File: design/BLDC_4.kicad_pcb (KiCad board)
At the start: 4 copper layers, 55 x 77 mm, 159 parts, among them J1 Conn_01x03, J2 Conn_01x02, J3 Conn_02x06_Odd_Even, J4 Conn_01x01_Pin, J5 Conn_01x01_Pin, J6 Conn_02x06_Odd_Even, K1 SERVO, P101 CANBUS, P2 SWD, P3 PWR_COMM, Q1 IRFS7530, Q2 IRFS7530, Q3 IRFS7530, Q4 IRFS7530, Q5 IRFS7530, Q6 IRFS7530, U1 STM32F40X_LQFP64, U2 TC2117, U3 DRV8302, U4 INA826AIDR, U401 SN65HVD232, U5 AM26LV32xD, U6 OPA333AIDBVR, U7 INA826AIDR, U8 MAX485ED, U9 OPA333AIDBVR, X1 MINI-USB-SHIELD-32005-201, X2 8MHz 10ppm

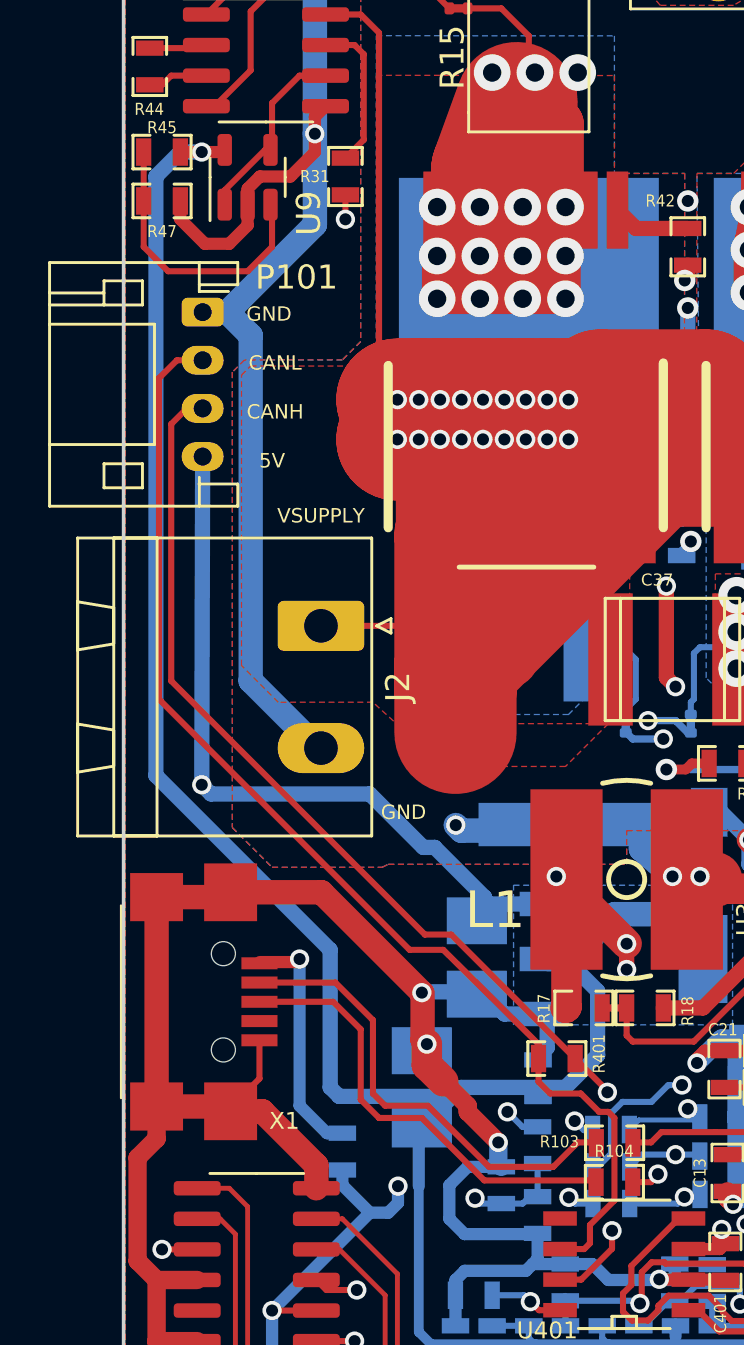
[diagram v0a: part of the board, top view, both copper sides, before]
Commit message: Changing to USB-C connector
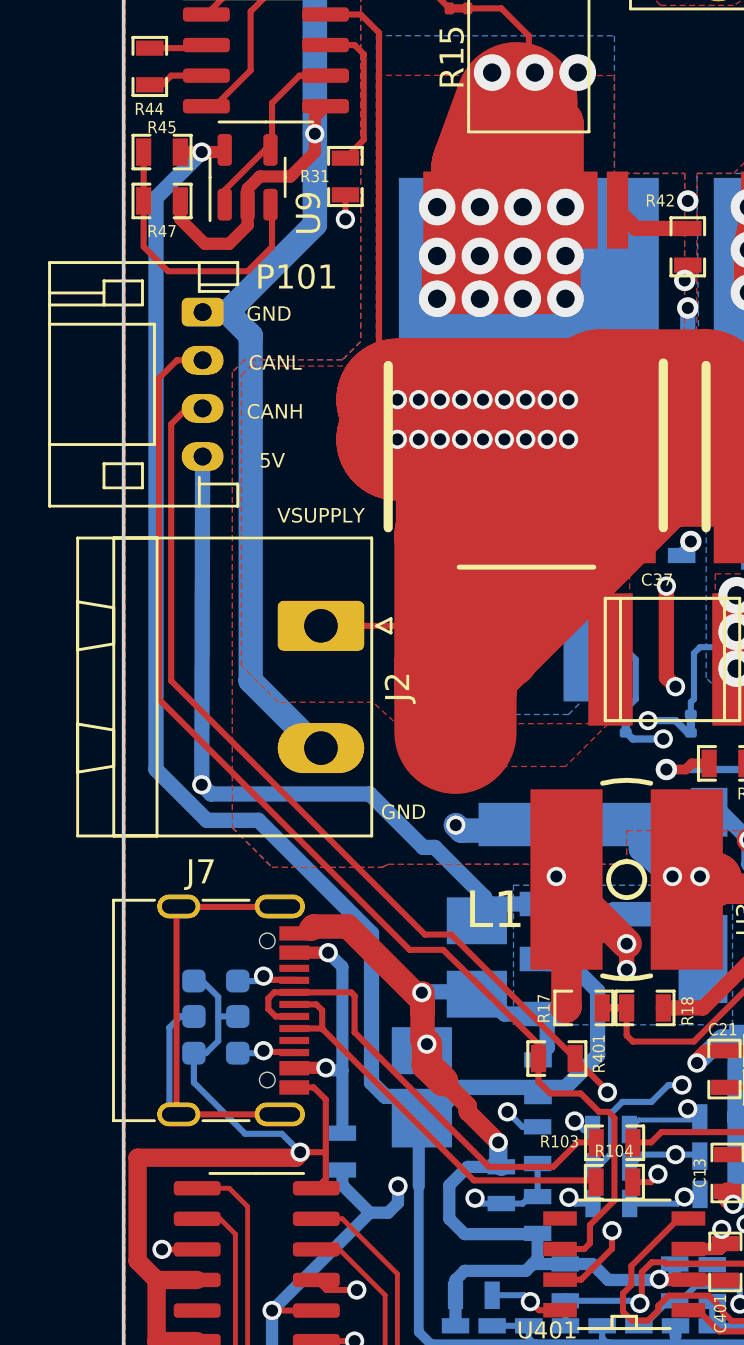
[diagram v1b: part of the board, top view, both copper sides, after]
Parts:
- removed X1: MINI-USB-SHIELD-32005-201, CRF1:USB-UX60R-MB-5ST
- added J7: USB_C_Receptacle_USB2.0, Connector_USB:USB_C_Receptacle_G-Switch_GT-USB-7010ASV, F.Cu at (71.4, 120.5)
- added R54: 4K7, Resistor_SMD:R_0603_1608Metric_Pad0.98x0.95mm_HandSolder, B.Cu at (71.8, 119.3)
- added R55: 4K7, Resistor_SMD:R_0603_1608Metric_Pad0.98x0.95mm_HandSolder, B.Cu at (71.8, 122.3)
- added R56: 100K, Resistor_SMD:R_0603_1608Metric_Pad0.98x0.95mm_HandSolder, B.Cu at (71.8, 120.8)
- R41, R44: value 39k -> 5.1k 0.1%
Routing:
- net Net-(J7-SHIELD): track 0.00 -> 22.2 mm
- net GND: track 582.5 -> 588.0 mm, vias 31 -> 32
- net Net-(J7-CC1): track 0.00 -> 2.54 mm, vias 0 -> 1
- net Net-(J7-CC2): track 0.00 -> 2.50 mm, vias 0 -> 1
- net Net-(J7-D+-PadA6): track 18.8 -> 17.3 mm
- net Net-(J7-VBUS-PadA4): track 10.1 -> 11.3 mm, vias 1 -> 2

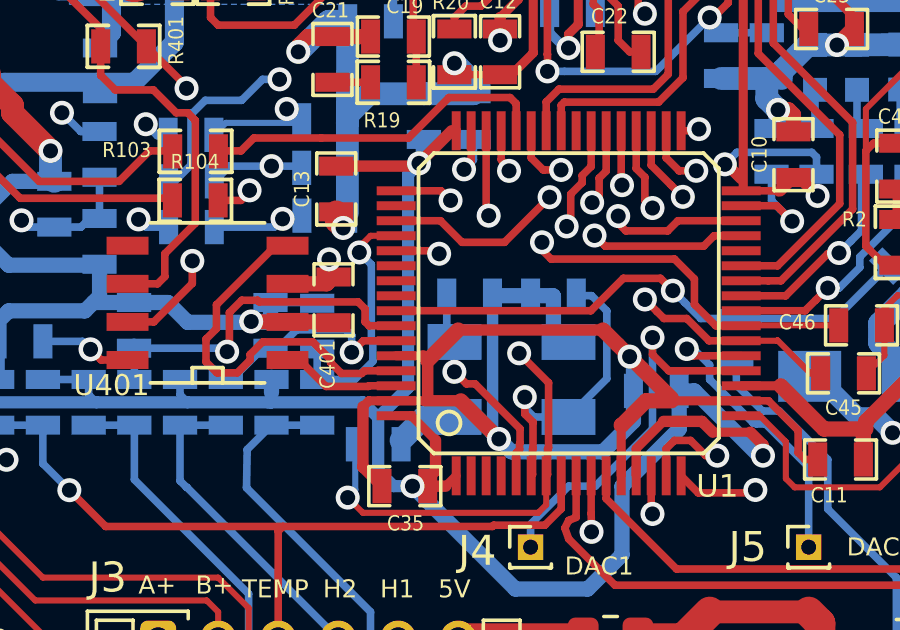
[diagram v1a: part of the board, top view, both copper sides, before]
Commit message: Swapped SERVO and SENS1 pins
Signed-off-by: Leonardo Celente <leocelente@gmail.com>
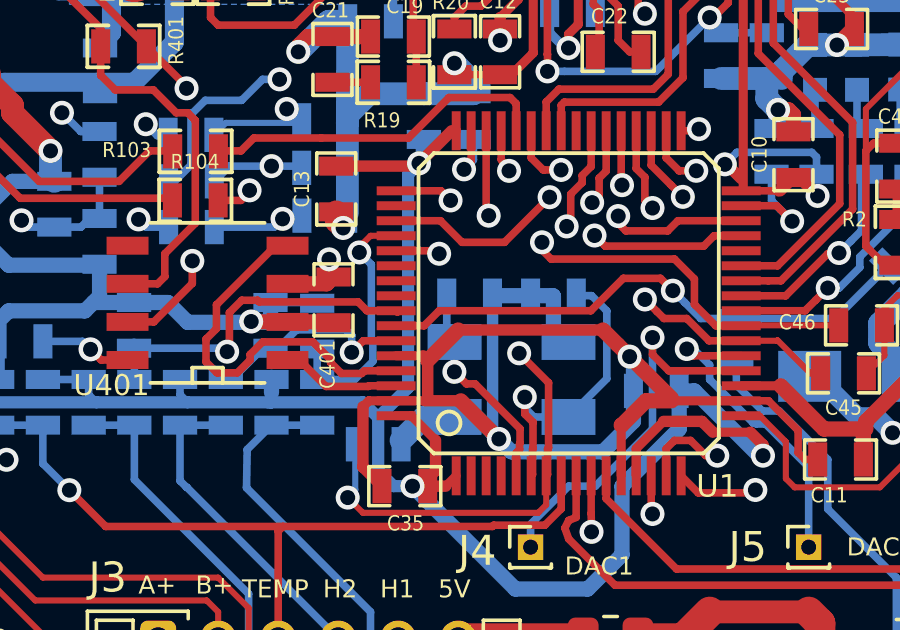
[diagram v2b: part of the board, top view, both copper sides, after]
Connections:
- U1 pad 57: /MCU/SERVO -> /Filters/HALL1_OUT
- U1 pad 58: /Filters/HALL1_OUT -> /MCU/SERVO
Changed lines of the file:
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@@
       (net 112 "unconnected-(U1-PB4(NJTRST)-Pad56)") (pinfunction "PB4(NJTRST)") (pintype "bidirectional+no_connect"))
     (pad "57" smd rect (at -5.75056 0.24892) (size 1.30048 0.3) (layers "F.Cu" "F.Paste" "F.Mask")
-      (net 144 "/MCU/SERVO") (pinfunction "PB5") (pintype "bidirectional"))
+      (net 71 "/Filters/HALL1_OUT") (pinfunction "PB5") (pintype "bidirectional"))
     (pad "58" smd rect (at -5.75056 0.7493) (size 1.30048 0.3) (layers "F.Cu" "F.Paste" "F.Mask")
-      (net 71 "/Filters/HALL1_OUT") (pinfunction "PB6") (pintype "bidirectional"))
+      (net 144 "/MCU/SERVO") (pinfunction "PB6") (pintype "bidirectional"))
     (pad "59" smd rect (at -5.75056 1.24968) (size 1.30048 0.3) (layers "F.Cu" "F.Paste" "F.Mask")
       (net 70 "/Filters/HALL2_OUT") (pinfunction "PB7") (pintype "bidirectional"))
@@
     (pts (xy 123 149) (xy 68 149))
     (height -3.971)
-    (gr_text "2165.3543 mils" (at 95.5 151.821) (layer "Dwgs.User")
+    (gr_text "55,0000 mm" (at 95.5 151.821) (layer "Dwgs.User")
       (effects (font (size 1 1) (thickness 0.15)))
     )
@@
     (pts (xy 68 70) (xy 68 147))
     (height 4.85)
-    (gr_text "3031.4961 mils" (at 62 108.5 90) (layer "Dwgs.User")
+    (gr_text "77,0000 mm" (at 62 108.5 90) (layer "Dwgs.User")
       (effects (font (size 1 1) (thickness 0.15)))
     )
@@
   (segment (start 90.646 132.562) (end 89.604 133.604) (width 0.254) (layer "B.Cu") (net 70))
   (segment (start 89.604 133.604) (end 89.408 133.604) (width 0.254) (layer "B.Cu") (net 70))
-  (segment (start 94.1832 131.8133) (end 94.05 131.6801) (width 0.254) (layer "F.Cu") (net 71))
-  (segment (start 89.528611 132.602261) (end 89.453446 132.677426) (width 0.254) (layer "F.Cu") (net 71))
-  (segment (start 89.940933 130.96399) (end 89.528611 131.376312) (width 0.254) (layer "F.Cu") (net 71))
-  (segment (start 90.523389 131.019521) (end 90.467858 130.96399) (width 0.254) (layer "F.Cu") (net 71))
-  (segment (start 89.528611 131.376312) (end 89.528611 132.602261) (width 0.254) (layer "F.Cu") (net 71))
-  (segment (start 93.819521 131.019521) (end 90.523389 131.019521) (width 0.254) (layer "F.Cu") (net 71))
-  (segment (start 94.05 131.25) (end 93.819521 131.019521) (width 0.254) (layer "F.Cu") (net 71))
-  (segment (start 94.05 131.6801) (end 94.05 131.25) (width 0.254) (layer "F.Cu") (net 71))
-  (segment (start 90.467858 130.96399) (end 89.940933 130.96399) (width 0.254) (layer "F.Cu") (net 71))
-  (segment (start 95.08744 131.8133) (end 94.1832 131.8133) (width 0.254) (layer "F.Cu") (net 71))
+  (segment (start 90.467858 130.96399) (end 90.523389 131.019521) (width 0.254) (layer "F.Cu") (net 71))
+  (segment (start 89.453446 132.677426) (end 89.528611 132.602261) (width 0.254) (layer "F.Cu") (net 71))
+  (segment (start 89.940933 130.96399) (end 90.467858 130.96399) (width 0.254) (layer "F.Cu") (net 71))
+  (segment (start 95.123 131.35342) (end 95.123 131.318) (width 0.254) (layer "F.Cu") (net 71))
+  (segment (start 94.11292 131.31292) (end 95.08744 131.31292) (width 0.254) (layer "F.Cu") (net 71))
+  (segment (start 93.819521 131.019521) (end 94.11292 131.31292) (width 0.254) (layer "F.Cu") (net 71))
+  (segment (start 89.528611 132.602261) (end 89.528611 131.376312) (width 0.254) (layer "F.Cu") (net 71))
+  (segment (start 95.12808 131.3585) (end 95.123 131.35342) (width 0.254) (layer "F.Cu") (net 71))
+  (segment (start 90.523389 131.019521) (end 93.819521 131.019521) (width 0.254) (layer "F.Cu") (net 71))
+  (segment (start 89.528611 131.376312) (end 89.940933 130.96399) (width 0.254) (layer "F.Cu") (net 71))
   (via (at 89.453446 132.677426) (size 0.8) (drill 0.5) (layers "F.Cu" "B.Cu") (net 71))
   (segment (start 86.35 132.562) (end 89.33802 132.562) (width 0.254) (layer "B.Cu") (net 71))
@@
   (segment (start 90.17 141.224) (end 90.17 143.129) (width 0.2032) (layer "F.Cu") (net 143))
   (segment (start 76.008 129.159) (end 77.089 129.159) (width 0.2032) (layer "F.Cu") (net 143))
-  (segment (start 103.899261 130.2322) (end 104.310799 130.643738) (width 0.254) (layer "F.Cu") (net 144))
-  (segment (start 102.658692 130.2322) (end 103.899261 130.2322) (width 0.254) (layer "F.Cu") (net 144))
-  (segment (start 95.12808 131.31292) (end 95.123 131.318) (width 0.254) (layer "F.Cu") (net 144))
-  (segment (start 101.577972 131.31292) (end 95.12808 131.31292) (width 0.254) (layer "F.Cu") (net 144))
-  (segment (start 101.577972 131.31292) (end 102.658692 130.2322) (width 0.254) (layer "F.Cu") (net 144))
+  (segment (start 96.01962 131.8133) (end 96.52 131.31292) (width 0.254) (layer "F.Cu") (net 144))
+  (segment (start 101.577972 131.31292) (end 96.52 131.31292) (width 0.254) (layer "F.Cu") (net 144))
+  (segment (start 102.658692 130.2322) (end 101.577972 131.31292) (width 0.254) (layer "F.Cu") (net 144))
+  (segment (start 95.08744 131.8133) (end 96.01962 131.8133) (width 0.254) (layer "F.Cu") (net 144))
+  (segment (start 104.310799 130.643738) (end 103.899261 130.2322) (width 0.254) (layer "F.Cu") (net 144))
+  (segment (start 103.899261 130.2322) (end 102.658692 130.2322) (width 0.254) (layer "F.Cu") (net 144))
   (via (at 104.310799 130.643738) (size 0.8) (drill 0.5) (layers "F.Cu" "B.Cu") (net 144))
   (segment (start 109.728 131.572) (end 107.2515 131.572) (width 0.254) (layer "B.Cu") (net 144))
